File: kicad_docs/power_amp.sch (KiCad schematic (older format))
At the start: 13 parts, among them T2 NSC041318, U4 6V6, U5 6V6

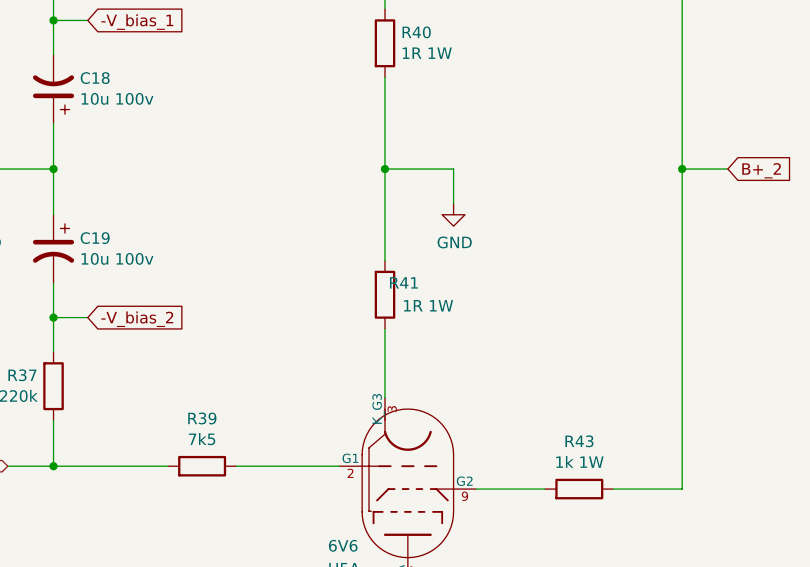
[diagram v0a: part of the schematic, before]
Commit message: add approximate voltages
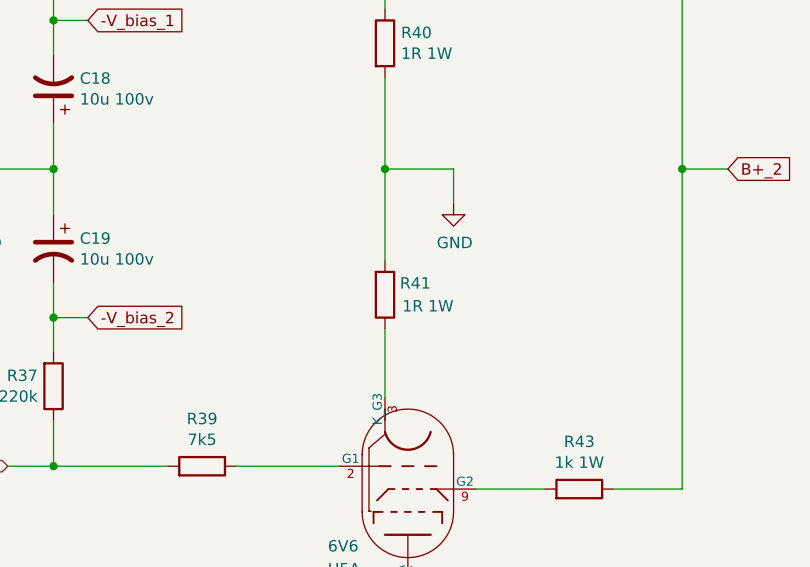
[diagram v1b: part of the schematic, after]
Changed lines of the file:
@@
 U 1 1 60DB77F8
 P 4850 4400
-F 0 "R41" H 5000 4350 50  0000 R CNN
+F 0 "R41" H 5050 4350 50  0000 R CNN
 F 1 "1R 1W" H 5150 4450 50  0000 R CNN
 F 2 "" V 4780 4400 50  0001 C CNN
